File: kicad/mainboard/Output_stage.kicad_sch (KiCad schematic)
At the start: 43 parts, among them J6 OUTPUT A, J7 OUTPUT B, T1 IRL520N, T2 IRL520N, T3 IRF9Z24, T4 IRL520N, T5 IRL520N, T6 IRF9Z24, U10 LM358N, U7 LTC1661, U8 MAX548A

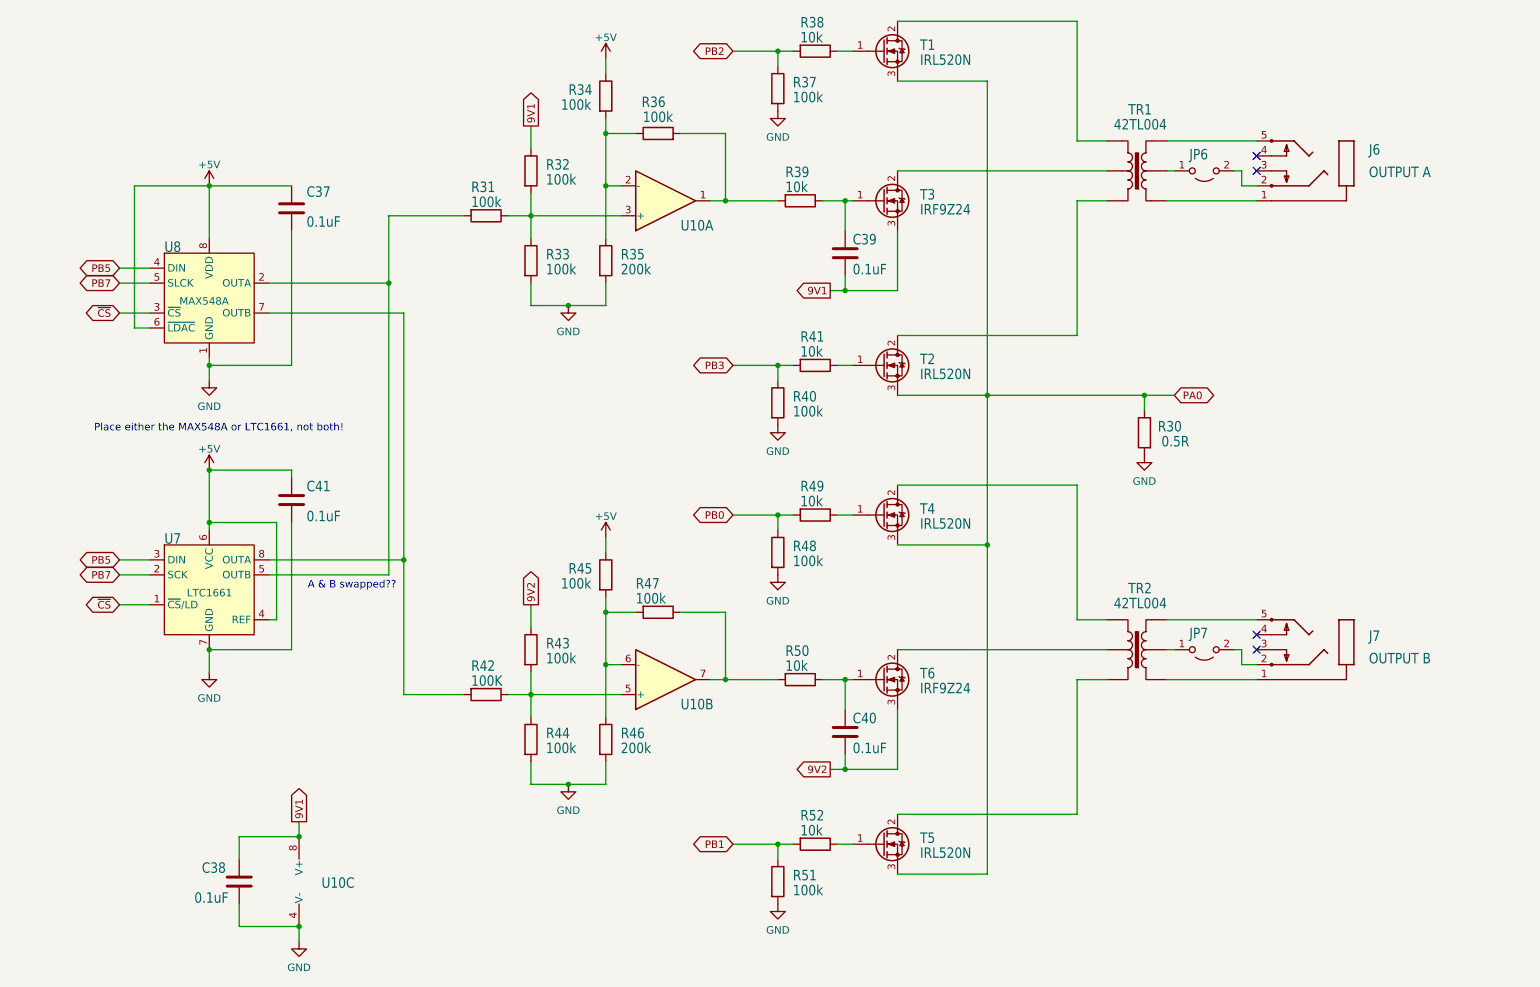
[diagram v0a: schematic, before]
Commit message: Bringing mainboard up to par with V1.4 schematics based on images. Rerouted a few lines since they could not pass below the MOSFETs due to a different footprint/pad size.
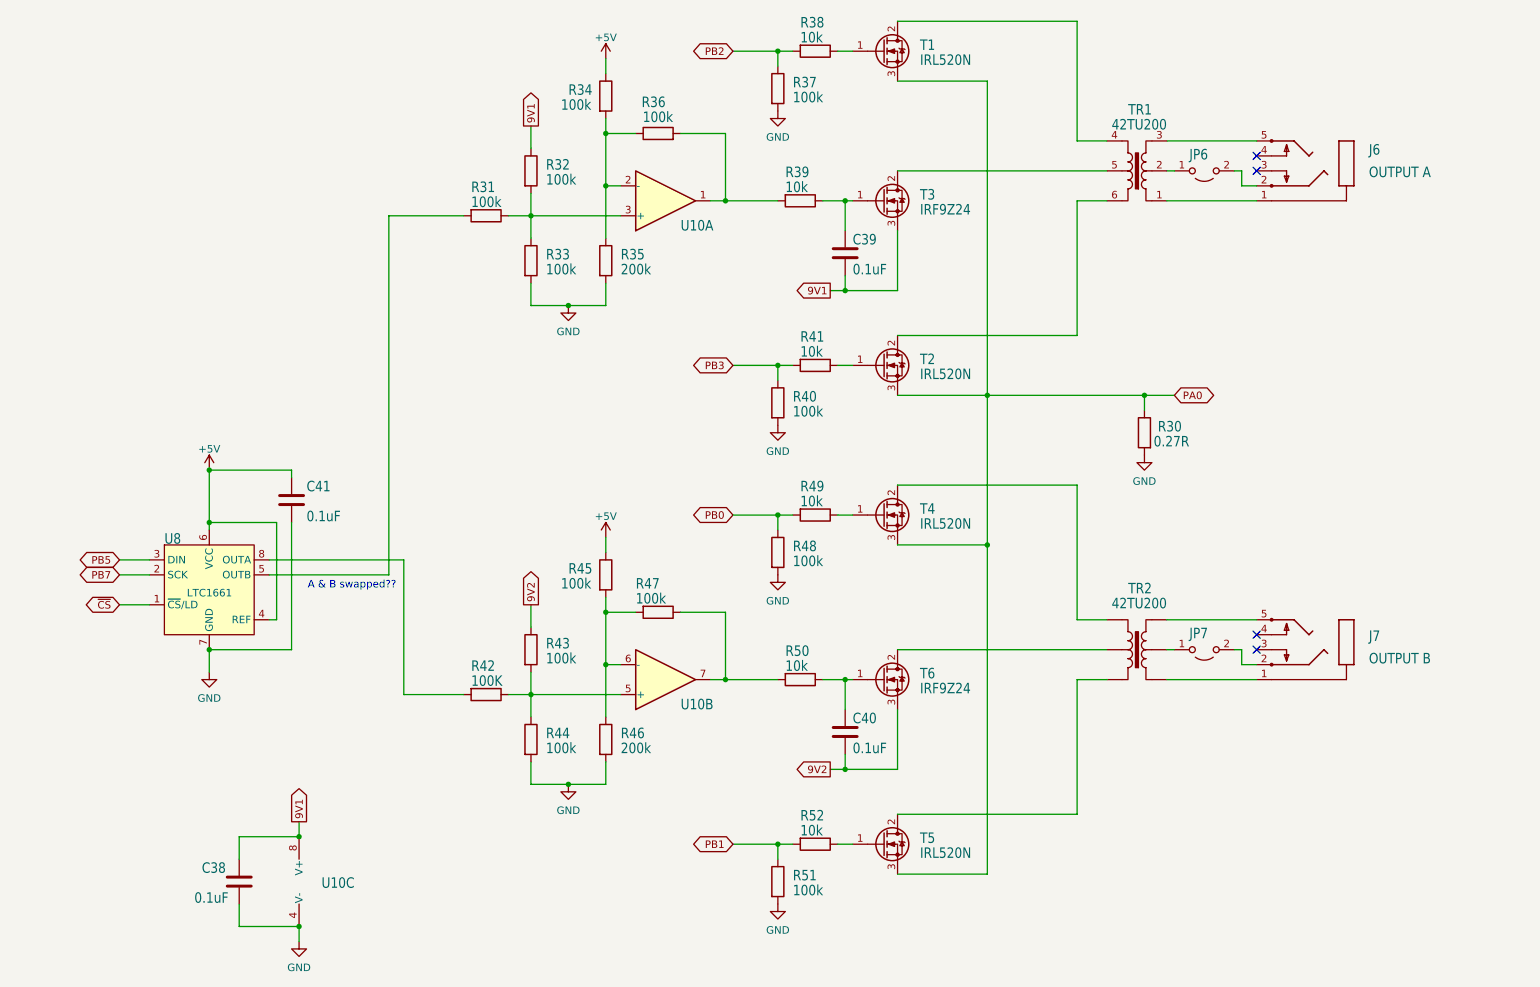
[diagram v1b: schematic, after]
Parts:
- removed C37: 0.1uF, Capacitor_THT:C_Disc_D3.0mm_W1.6mm_P2.50mm, symbol Device:C
- removed U8: MAX548A, Package_DIP:DIP-8_W7.62mm, symbol mk312-eagle-import:MAX548A
- R30: value 0.5R -> 0.27R
- R37, R38, R40, R41, R48, R49, R51, R52: footprint Resistor_THT:R_Axial_DIN0207_L6.3mm_D2.5mm_P10.16mm_Horizontal -> Resistor_THT:R_Axial_DIN0207_L6.3mm_D2.5mm_P2.54mm_Vertical
- TR1, TR2: value 42TL004 -> 42TU200; footprint mk312:42TL -> mk312:Transformer_Xicon_42TU
- renumbered U7 to U8
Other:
- note removed: "Place either the MAX548A or LTC1661, not both!"

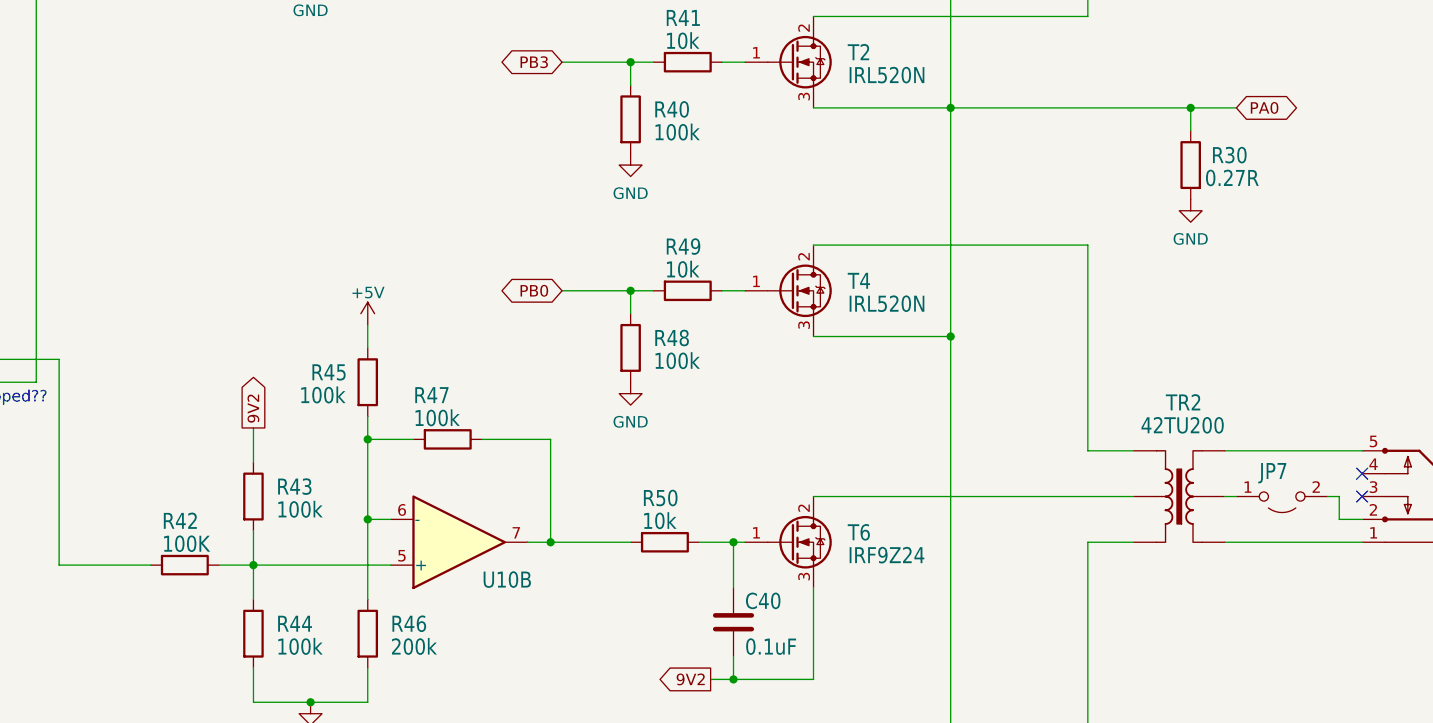
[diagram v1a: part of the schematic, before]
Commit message: Brought component numbers back in line with the original schematics
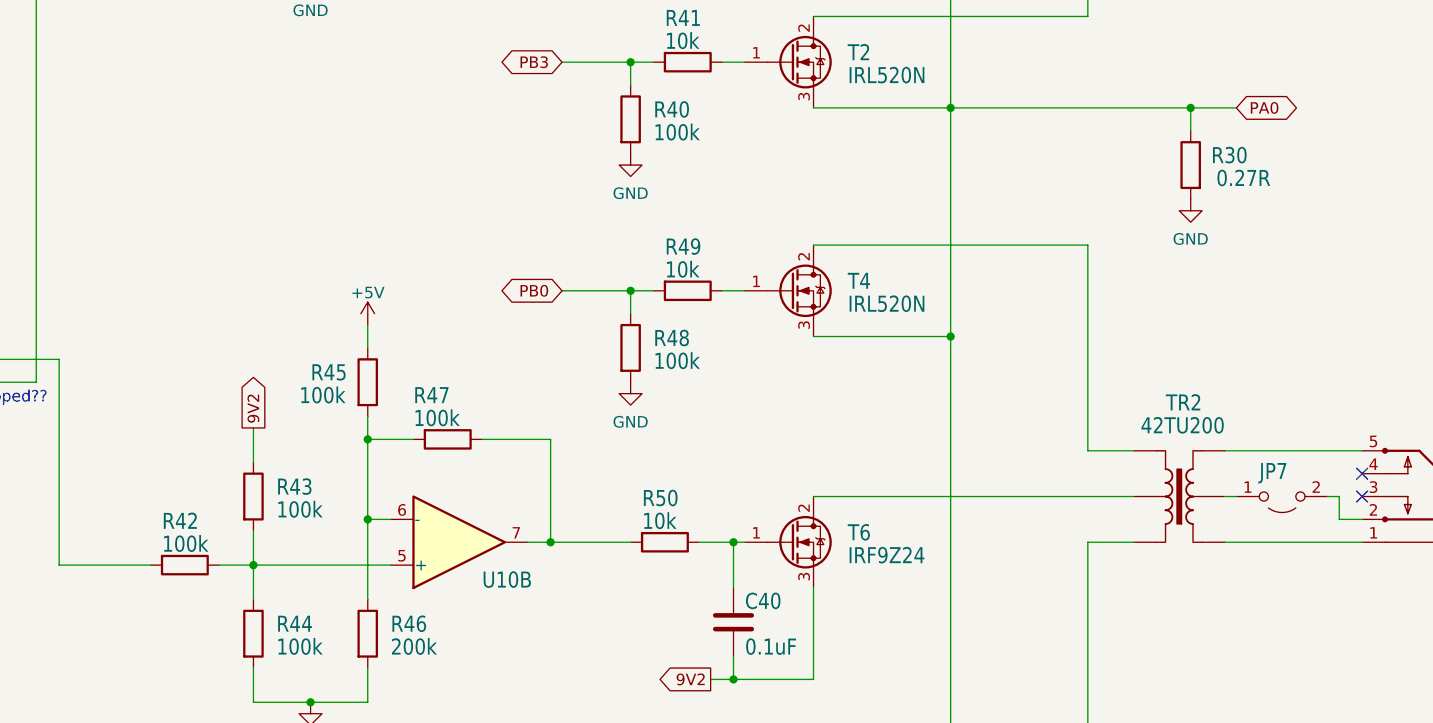
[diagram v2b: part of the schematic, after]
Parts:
- R42: value 100K -> 100k
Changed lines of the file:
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@@
       (effects (font (size 1.778 1.5113)) (justify left bottom))
     )
-    (property "Value" "0.27R" (id 1) (at 224.79 91.44 0)
+    (property "Value" "0.27R" (id 1) (at 226.06 91.44 0)
       (effects (font (size 1.778 1.5113)) (justify left bottom))
     )
@@
       (effects (font (size 1.778 1.5113)) (justify left bottom))
     )
-    (property "Value" "100K" (id 1) (at 102.87 132.08 90)
+    (property "Value" "100k" (id 1) (at 102.87 132.08 90)
       (effects (font (size 1.778 1.5113)) (justify left bottom))
     )

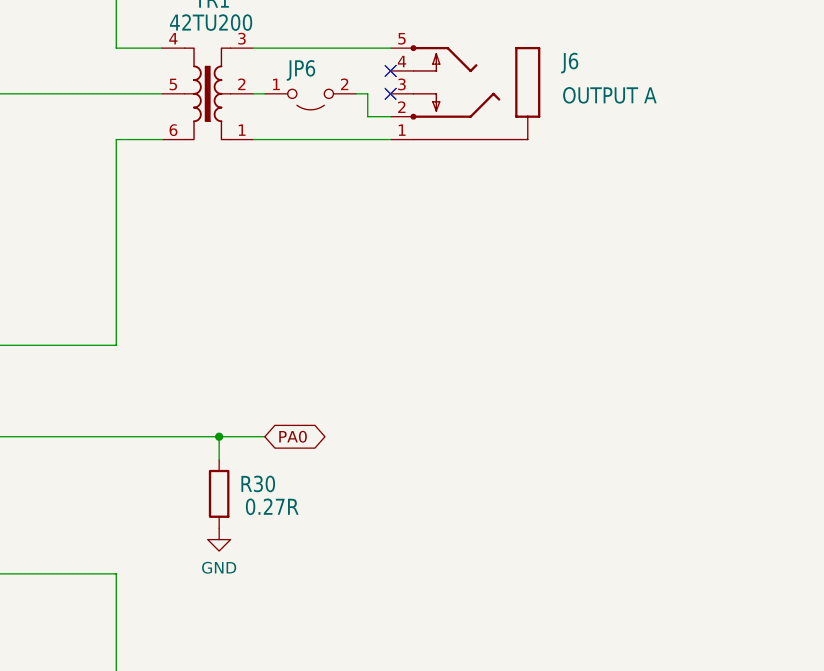
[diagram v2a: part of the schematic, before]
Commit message: Putting in new combined footprint for transformer. Updated F.Fab layer with component values in the correct place
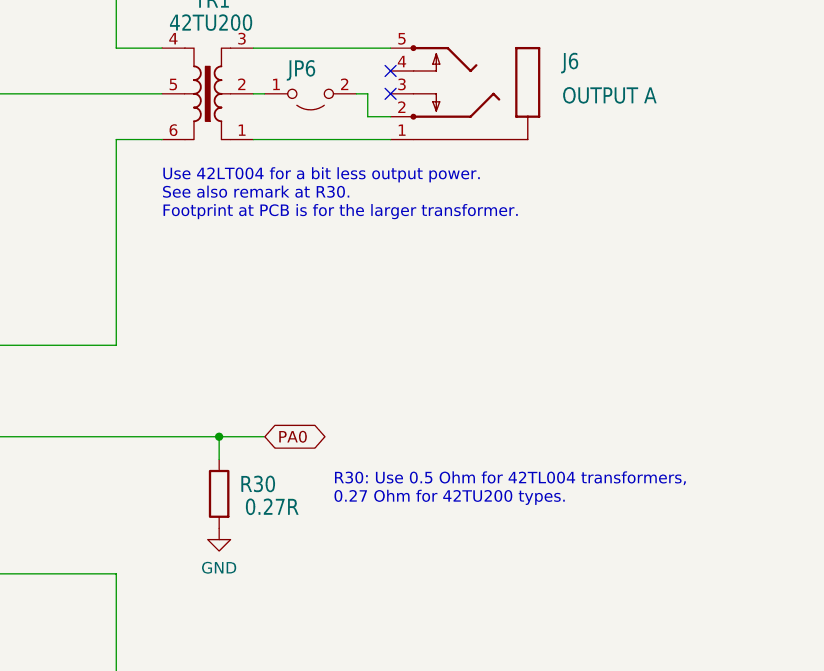
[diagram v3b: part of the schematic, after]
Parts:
- TR1, TR2: footprint mk312:Transformer_Xicon_42TU -> mk312:Transformer_Xicon_42TL_42TU_Combi
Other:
- note added: "R30: Use 0.5 Ohm for 42TL004 transformers, 0.27 Ohm for 42TU200 types."
- note added: "Use 42LT004 for a bit less output power. See also remark at R30. Footprint at PCB is for the larger transformer."
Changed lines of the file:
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@@
     (effects (font (size 1.27 1.27)) (justify right bottom))
+  )
+  (text "R30: Use 0.5 Ohm for 42TL004 transformers, \n0.27 Ohm for 42TU200 types."
+    (at 229.87 90.17 0)
+    (effects (font (size 1.27 1.27)) (justify left bottom))
+  )
+  (text "Use 42LT004 for a bit less output power. \nSee also remark at R30.\nFootprint at PCB is for the larger transformer."
+    (at 210.82 58.42 0)
+    (effects (font (size 1.27 1.27)) (justify left bottom))
   )
   (global_label "9V2" (shape output) (at 163.83 146.05 180) (fields_autoplaced)
@@
       (effects (font (size 1.778 1.5113)) (justify left bottom))
     )
-    (property "Footprint" "mk312:Transformer_Xicon_42TU" (id 2) (at 215.9 44.45 0)
+    (property "Footprint" "mk312:Transformer_Xicon_42TL_42TU_Combi" (id 2) (at 215.9 44.45 0)
       (effects (font (size 1.27 1.27)) hide)
     )
@@
       (effects (font (size 1.778 1.5113)) (justify left bottom))
     )
-    (property "Footprint" "mk312:Transformer_Xicon_42TU" (id 2) (at 215.9 125.73 0)
-      (effects (font (size 1.27 1.27)) hide)
-    )
+    (property "Footprint" "mk312:Transformer_Xicon_42TL_42TU_Combi" (id 2) (at 215.9 125.73 0)
+      (effects (font (size 1.27 1.27)) hide)
+    )

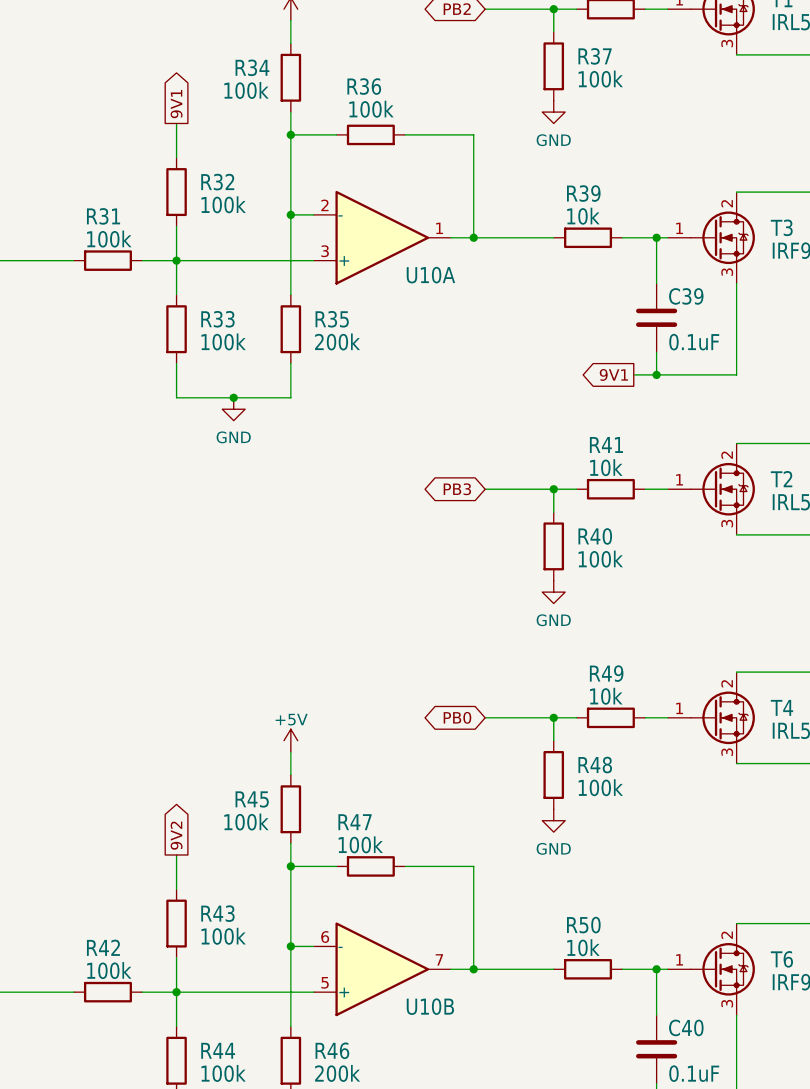
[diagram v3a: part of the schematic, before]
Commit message: A bit of cleanup, showing type of some OpAmps and clarification of wiring around U4
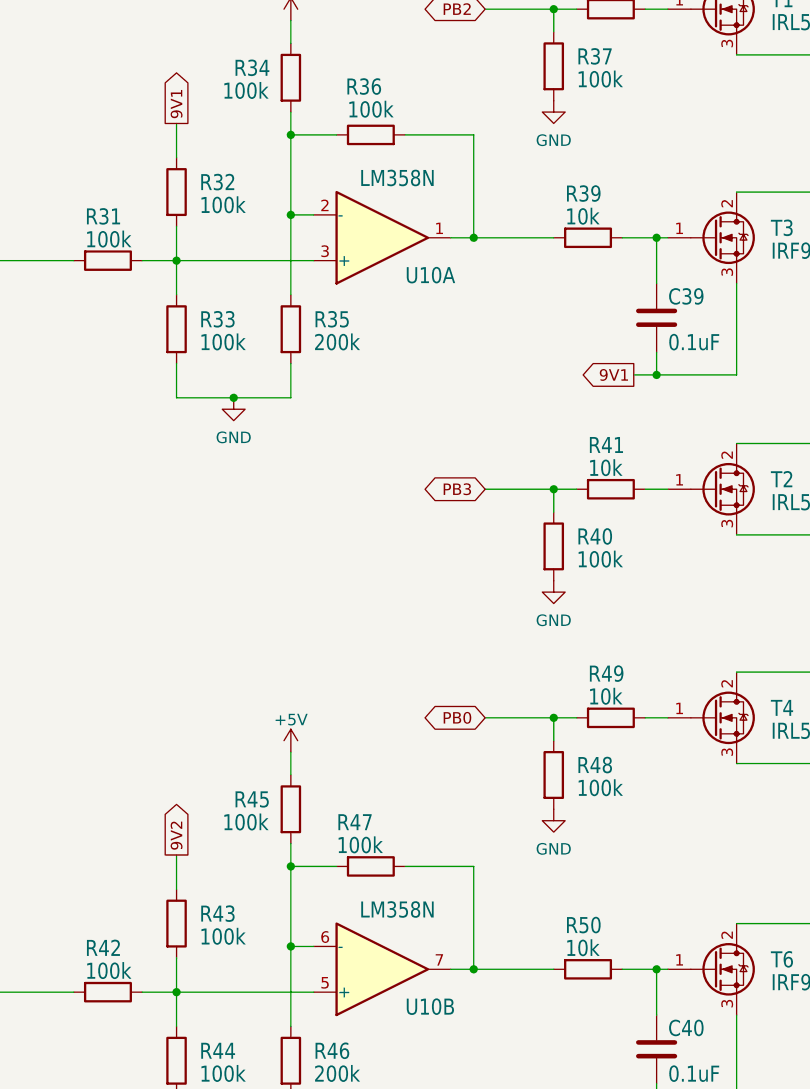
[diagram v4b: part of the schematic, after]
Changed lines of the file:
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@@
       (effects (font (size 1.778 1.5113)) (justify left bottom))
     )
-    (property "Value" "LM358N" (id 1) (at 138.43 44.45 0)
-      (effects (font (size 1.778 1.5113)) (justify left bottom) hide)
+    (property "Value" "LM358N" (id 1) (at 133.35 41.91 0)
+      (effects (font (size 1.778 1.5113)) (justify left bottom))
     )
     (property "Footprint" "Package_DIP:DIP-8_W7.62mm" (id 2) (at 135.89 49.53 0)
@@
       (effects (font (size 1.778 1.5113)) (justify left bottom))
     )
-    (property "Value" "LM358N" (id 1) (at 138.43 125.73 0)
-      (effects (font (size 1.778 1.5113)) (justify left bottom) hide)
+    (property "Value" "LM358N" (id 1) (at 133.35 123.19 0)
+      (effects (font (size 1.778 1.5113)) (justify left bottom))
     )
     (property "Footprint" "Package_DIP:DIP-8_W7.62mm" (id 2) (at 135.89 130.81 0)
